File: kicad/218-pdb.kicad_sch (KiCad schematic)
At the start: 79 parts, among them J1 Conn_01x03, J10 Conn_01x03, J11 Conn_01x03, J12 Conn_01x03, J13 Conn_01x03, J14 Conn_01x03, J15 Conn_01x03, J16 Conn_01x03, J17 Conn_01x03, J18 Conn_01x03, J19 Conn_01x03, J2 Conn_01x03, J20 Conn_01x03, J21 Conn_01x03, J22 Conn_01x03, J23 Conn_01x03, J24 Conn_01x03, J25 Conn_01x04_Pin, J26 Conn_01x04_Pin, J27 external 5V, J28 battery, J29 battery, J3 Conn_01x03, J30 battery, J31 battery, J32 battery, J33 battery, J4 Conn_01x03, J5 Conn_01x03, J6 Conn_01x03, J7 Conn_01x03, J8 Conn_01x03, J9 Conn_01x03, SW1 5V switch, U1 TLV76133DCY, U2 DC-DC buck, U3 TLV76133DCY, U4 DC-DC buck, U5 TLV76150DCY, U6 TLV76150DCY

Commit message: update bom
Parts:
- H1, H2, H3, H4: now fitted
- J28, J29, J30, J31: value battery -> 14v
- NT1: Part_Number (none) -> 2x3 header pins
- TP5-1,2, TP5-3: now left out of the parts list
- U1, U3: Part_Number (none) -> TLV76133DCY
- U5, U6: Part_Number (none) -> TLV76150DCY

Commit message: adjust layout
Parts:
- renumbered TP5-1,2 to TP-U1, TP5-3 to TP-U2, U4 to U1, U1 to U3, U3 to U4
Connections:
- net GND: now also R5.1; no longer R5.2
- net at D6.1 (K): now also R5.2; no longer R5.1
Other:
- moved on the sheet: C5, C6, C7, C8, D10, D2, D4, D6, J27, J28, J29, J30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

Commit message: add fuse terminal
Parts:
- added Fuse1: fuse, 218-pdb:CUI_TB007-508-02BE, symbol 218-pdb:Conn_01x02
- FID1, FID2, FID3, FID4: value one 90 degree header pin -> 90 degree header pin; Part_Number (none) -> 90 degree header pin
- NT2: symbol Switch:SW_SPDT -> Switch:SW_SPDT_321
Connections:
- net +BATT: now also Fuse1.1 (Pin_1); no longer J32.1 (Pin_1)
- net 14-1: now also NT2.1 (C); no longer NT2.3 (C)
- net 14-3: now also NT2.3 (A); no longer NT2.1 (A)
- new net: Fuse1.2 (Pin_2), J32.1 (Pin_1)
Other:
- note added: "14 volt power"
- note added: "14v motor power"
- note added: "3.3 volt regulators"
- note added: "5-1"
- note added: "5-2"
- note added: "5V switch"
- note added: "M3 bolt holes 91.440mm by 66.040mm"
- note added: "battery"
- note added: "battery to 5 volt regulators"
- note added: "external"
- note added: "main switch"
- note added: "power switches and servo power selector"
- note added: "row 1"
- note added: "row 2"
- note added: "row 3 servo power"
- note added: "selector"
- note added: "servo power"
- note added: "servo pwr"
- note added: "servo regulator"
- moved on the sheet: D10, D6, H1, H2, H3, H4, J1, J10, J11, J12, J13, J14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

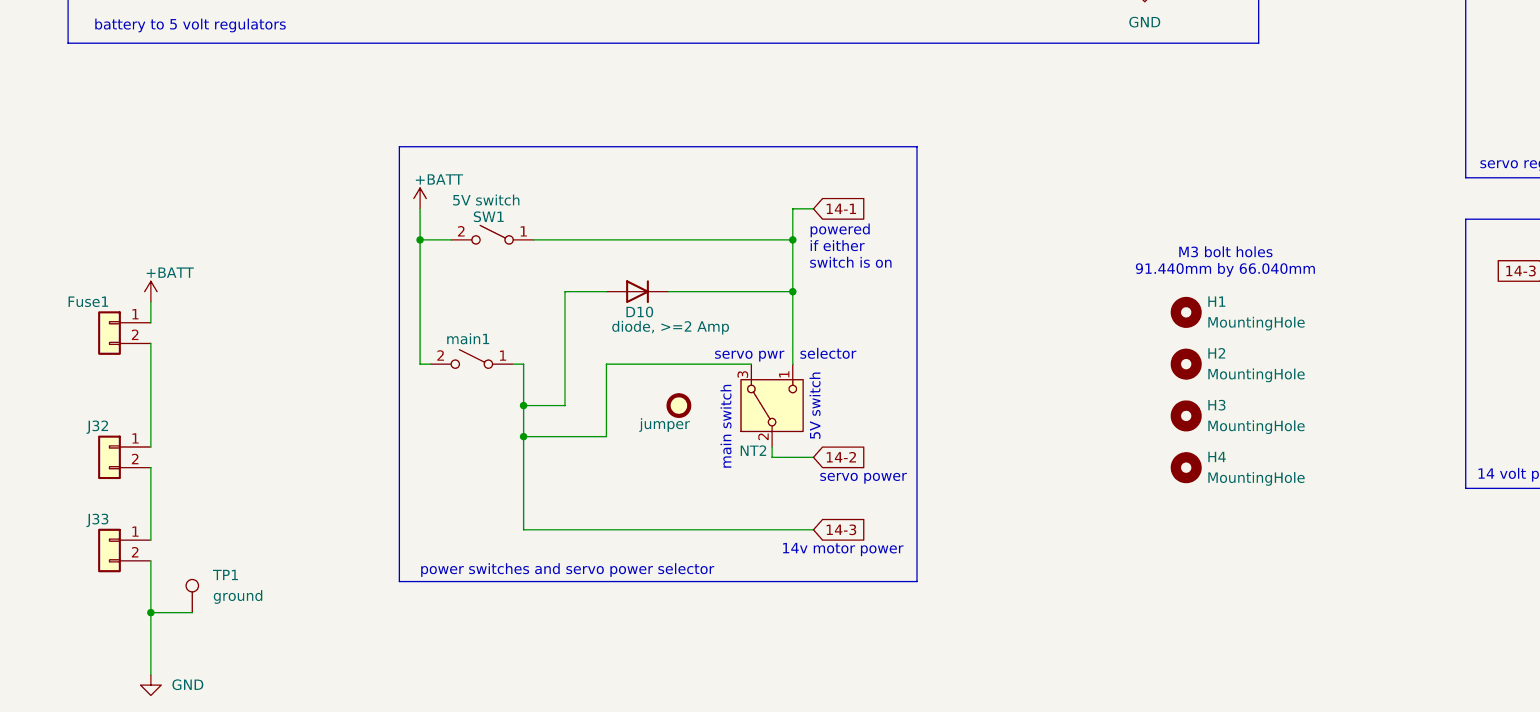
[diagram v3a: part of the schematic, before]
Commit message: align silkscreen and comment schematic
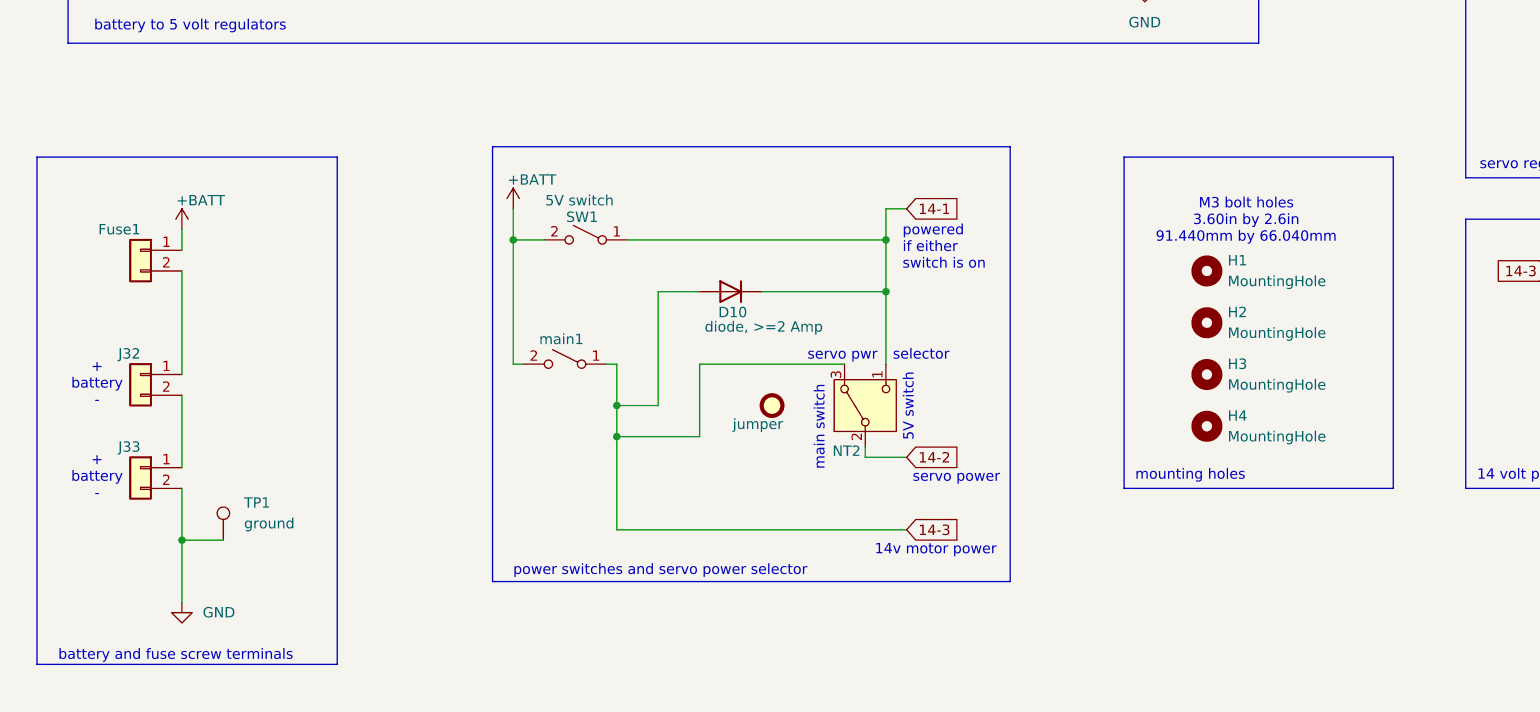
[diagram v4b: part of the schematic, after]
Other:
- note added: "+ battery -"
- note added: "M3 bolt holes 3.60in by 2.6in 91.440mm by 66.040mm"
- note added: "battery and fuse screw terminals"
- note added: "mounting holes"
- note removed: "M3 bolt holes 91.440mm by 66.040mm"
- moved on the sheet: D10, Fuse1, H1, H2, H3, H4, J32, J33, NT2, SW1, TP1, main1

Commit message: change jst xh model
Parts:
- J1, J10, J11, J12, J13, J14, J15, J16, J2, J3, J4, J5, J6, J7, J8, J9: footprint 218-pdb:JST_XH_B3B-XH-A_1x03_P2.50mm_Vertical -> 218-pdb:JST_XH_B3B-XH-AM_1x03_P2.50mm_Vertical
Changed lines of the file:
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@@
 			)
 		)
-		(property "Footprint" "218-pdb:JST_XH_B3B-XH-A_1x03_P2.50mm_Vertical"
+		(property "Footprint" "218-pdb:JST_XH_B3B-XH-AM_1x03_P2.50mm_Vertical"
 			(at 190.5 25.4 0)
 			(effects
@@
 			)
 		)
-		(property "Footprint" "218-pdb:JST_XH_B3B-XH-A_1x03_P2.50mm_Vertical"
+		(property "Footprint" "218-pdb:JST_XH_B3B-XH-AM_1x03_P2.50mm_Vertical"
 			(at 262.89 25.4 0)
 			(effects
@@
 			)
 		)
-		(property "Footprint" "218-pdb:JST_XH_B3B-XH-A_1x03_P2.50mm_Vertical"
+		(property "Footprint" "218-pdb:JST_XH_B3B-XH-AM_1x03_P2.50mm_Vertical"
 			(at 212.09 41.91 0)
 			(effects
@@
 			)
 		)
-		(property "Footprint" "218-pdb:JST_XH_B3B-XH-A_1x03_P2.50mm_Vertical"
+		(property "Footprint" "218-pdb:JST_XH_B3B-XH-AM_1x03_P2.50mm_Vertical"
 			(at 242.57 41.91 0)
 			(effects
@@
 			)
 		)
-		(property "Footprint" "218-pdb:JST_XH_B3B-XH-A_1x03_P2.50mm_Vertical"
+		(property "Footprint" "218-pdb:JST_XH_B3B-XH-AM_1x03_P2.50mm_Vertical"
 			(at 232.41 41.91 0)
 			(effects
@@
 			)
 		)
-		(property "Footprint" "218-pdb:JST_XH_B3B-XH-A_1x03_P2.50mm_Vertical"
+		(property "Footprint" "218-pdb:JST_XH_B3B-XH-AM_1x03_P2.50mm_Vertical"
 			(at 232.41 25.4 0)
 			(effects
@@
 			)
 		)
-		(property "Footprint" "218-pdb:JST_XH_B3B-XH-A_1x03_P2.50mm_Vertical"
+		(property "Footprint" "218-pdb:JST_XH_B3B-XH-AM_1x03_P2.50mm_Vertical"
 			(at 252.73 41.91 0)
 			(effects
@@
 			)
 		)
-		(property "Footprint" "218-pdb:JST_XH_B3B-XH-A_1x03_P2.50mm_Vertical"
+		(property "Footprint" "218-pdb:JST_XH_B3B-XH-AM_1x03_P2.50mm_Vertical"
 			(at 212.09 25.4 0)
 			(effects
@@
 			)
 		)
-		(property "Footprint" "218-pdb:JST_XH_B3B-XH-A_1x03_P2.50mm_Vertical"
+		(property "Footprint" "218-pdb:JST_XH_B3B-XH-AM_1x03_P2.50mm_Vertical"
 			(at 222.25 25.4 0)
 			(effects
@@
 			)
 		)
-		(property "Footprint" "218-pdb:JST_XH_B3B-XH-A_1x03_P2.50mm_Vertical"
+		(property "Footprint" "218-pdb:JST_XH_B3B-XH-AM_1x03_P2.50mm_Vertical"
 			(at 222.25 41.91 0)
 			(effects
@@
 			)
 		)
-		(property "Footprint" "218-pdb:JST_XH_B3B-XH-A_1x03_P2.50mm_Vertical"
+		(property "Footprint" "218-pdb:JST_XH_B3B-XH-AM_1x03_P2.50mm_Vertical"
 			(at 200.66 41.91 0)
 			(effects
@@
 			)
 		)
-		(property "Footprint" "218-pdb:JST_XH_B3B-XH-A_1x03_P2.50mm_Vertical"
+		(property "Footprint" "218-pdb:JST_XH_B3B-XH-AM_1x03_P2.50mm_Vertical"
 			(at 262.89 41.91 0)
 			(effects
@@
 			)
 		)
-		(property "Footprint" "218-pdb:JST_XH_B3B-XH-A_1x03_P2.50mm_Vertical"
+		(property "Footprint" "218-pdb:JST_XH_B3B-XH-AM_1x03_P2.50mm_Vertical"
 			(at 252.73 25.4 0)
 			(effects
@@
 			)
 		)
-		(property "Footprint" "218-pdb:JST_XH_B3B-XH-A_1x03_P2.50mm_Vertical"
+		(property "Footprint" "218-pdb:JST_XH_B3B-XH-AM_1x03_P2.50mm_Vertical"
 			(at 242.57 25.4 0)
 			(effects
@@
 			)
 		)
-		(property "Footprint" "218-pdb:JST_XH_B3B-XH-A_1x03_P2.50mm_Vertical"
+		(property "Footprint" "218-pdb:JST_XH_B3B-XH-AM_1x03_P2.50mm_Vertical"
 			(at 190.5 41.91 0)
 			(effects
@@
 			)
 		)
-		(property "Footprint" "218-pdb:JST_XH_B3B-XH-A_1x03_P2.50mm_Vertical"
+		(property "Footprint" "218-pdb:JST_XH_B3B-XH-AM_1x03_P2.50mm_Vertical"
 			(at 200.66 25.4 0)
 			(effects

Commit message: advice from Karl
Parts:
- C9: value 10 uF -> 220 uF; footprint Capacitor_THT:C_Disc_D3.8mm_W2.6mm_P2.50mm -> Capacitor_THT:CP_Radial_D5.0mm_P2.50mm; Part_Number 10uF tantalum (polarized) capacitor -> 220uf electrolytic
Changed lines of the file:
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@@
 			)
 		)
-		(property "Value" "10 uF"
+		(property "Value" "220 uF"
 			(at 243.84 118.4909 0)
 			(effects
@@
 			)
 		)
-		(property "Footprint" "Capacitor_THT:C_Disc_D3.8mm_W2.6mm_P2.50mm"
+		(property "Footprint" "Capacitor_THT:CP_Radial_D5.0mm_P2.50mm"
 			(at 240.9952 121.92 0)
 			(effects
@@
 			)
 		)
-		(property "Part_Number" "10uF tantalum (polarized) capacitor"
+		(property "Part_Number" "220uf electrolytic"
 			(at 240.03 118.11 0)
 			(effects
